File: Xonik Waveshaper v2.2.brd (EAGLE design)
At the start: 63.5 x 29.1 mm, 93 parts, among them IC1 TL074D, IC2 TL074D, IC3 TL074D, IC4 TL072D, IC5 4013D, IC6 LM311D, T1 2n3904

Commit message: Reduced footprints for op amps
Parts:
- added C15, C17, C18, C19: 1uF, rcl:C0402
- IC1, IC2, IC3: value TL074D -> TL074JT; device linear:SO14 -> joakim:TSSOP14J
- IC6: value LM311D -> LM311T; device linear:SO08 -> joakim:TSSOP8J
- moved IC6 78.2 mm to (51.4, 16.8), turned to 90 degrees
- moved C13 71.6 mm to (40.3, 21.7), turned to 90 degrees
- moved C12 59.1 mm to (23.5, 21.7), turned to 90 degrees
- moved C9 49.9 mm to (8.89, 21.7), turned to 90 degrees
- moved C16 12.6 mm to (40.4, 11.9), turned to 90 degrees
- moved C10 7.23 mm to (23.5, 11.9), turned to 90 degrees
- moved C11 7.19 mm to (8.89, 11.9), turned to 90 degrees
- moved 15 4.92 mm to (7.14, 24.8)
- moved +12V 2.54 mm to (49.5, 3.49)
- moved -12V 2.54 mm to (52.1, 3.49)
- moved GND 2.54 mm to (54.6, 3.49)
- moved IC4 1.84 mm to (46.7, 16.8)
- moved T1 1.59 mm to (4.13, 16.8)
- moved 13 1.11 mm to (10.6, 24.8)
- moved 5 1.11 mm to (10.6, 9.21)
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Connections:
- net N$20 renamed SS2_TRIM_R
- net N$23 renamed SS1_TRIM_L
- net N$28 renamed SS2_TRIM_L
- net N$33 renamed PW_CV
- net N$41 renamed SS1_TRIM_R
- net +12V: now also C15.2, C18.2
- net -12V: now also C17.1, C19.1
- net GND: now also C15.1, C17.2, C18.1, C19.2
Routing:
- net N$14: track 31.7 -> 36.9 mm
- net -12V: track 70.8 -> 75.7 mm
- net N$19: track 21.6 -> 24.8 mm
- net N$3: track 12.9 -> 9.76 mm
- net SUB_SAW_1: track 30.9 -> 33.6 mm
- net GND: track 256.1 -> 253.9 mm
- net N$13: track 19.0 -> 17.0 mm
- net SS2_TRIM_R: track 20.3 -> 22.2 mm
- net +12V: track 88.9 -> 90.7 mm
- net N$24: track 24.9 -> 23.1 mm
- net PULSE: track 23.3 -> 24.7 mm
- net TRIANGLE: track 33.0 -> 34.2 mm
- net N$12: track 11.2 -> 12.3 mm
- net N$4: track 21.2 -> 20.2 mm
- net SUB_SAW_2: track 24.1 -> 25.1 mm
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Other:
- board size 63.5 x 29.1 mm -> 63.5 x 29.3 mm

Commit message: Almost all tracing done!
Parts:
- 22: device resistor:R0805 -> rcl:R0603
- C1, C14, C2, C3, C4, C5, C6, C7: device rcl:C0603 -> joakim:R0603-J
- IC4: value TL072D -> TL072JT; device joakim:SO08J -> joakim:TSSOP8J
- IC5: value 4013D -> 4013T; device joakim:SO14J -> joakim:TSSOP14J
- moved 33 91.2 mm to (52.2, 10.5), turned to 90 degrees
- moved 1 91.1 mm to (48.7, 23.2), turned to 270 degrees
- moved C14 88.9 mm to (51.0, 23.2), turned to 90 degrees
- moved 2 86.1 mm to (50.0, 10.5), turned to 270 degrees
- moved 32 50.3 mm to (37.6, 10.5), turned to 270 degrees
- moved 21 33.2 mm to (17.5, 10.5), turned to 90 degrees
- moved 31 26.4 mm to (12.5, 10.5), turned to 270 degrees
- moved 9 21.1 mm to (12.5, 14.0), turned to 270 degrees
- moved 7 17.4 mm to (2.22, 19.1), turned to 0 degrees
- moved C8 17.1 mm to (48.4, 19.2), turned to 270 degrees
- moved 26 15.6 mm to (44.3, 23.2), turned to 270 degrees
- moved 8 15.1 mm to (2.22, 16.8), turned to 180 degrees
- moved 29 14.5 mm to (42.1, 23.2)
- moved C2 14.2 mm to (39.8, 23.2)
- moved C7 13.8 mm to (2.22, 14.6), turned to 180 degrees
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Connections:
- net GND: now also IC1.5; no longer IC1.3
- net INV_SAW: now also IC1.7; no longer IC1.1
- net N$1: now also IC2.2; no longer IC2.6
- net N$10: now also IC1.6; no longer IC1.2
- net N$15: now also IC2.6; no longer IC2.2
- net N$42: now also IC2.1; no longer IC2.7
- net N$5: now also IC1.3; no longer IC1.5
- net N$6: now also IC1.2; no longer IC1.6
- net PULSE: now also IC1.1; no longer IC1.7
- net SAW: now also IC2.7; no longer IC2.1
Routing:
- net GND: track 253.9 -> 42.4 mm, vias 22 -> 34
- net SUB_SAW_1: track 33.6 -> 5.00 mm, vias 2 -> 0
- net N$14: track 36.9 -> 9.64 mm
- net INV_SAW: track 50.2 -> 23.3 mm
- net N$35: track 46.5 -> 20.1 mm, vias 2 -> 0
- net SUB_SQR_1: track 47.1 -> 23.8 mm
- net SS2_TRIM_R: track 22.2 -> 0.00 mm, vias 2 -> 0
- net SS1_TRIM_R: track 23.7 -> 2.76 mm, vias 1 -> 0
- net SINE: track 35.7 -> 14.9 mm, vias 3 -> 2
- net SUB_SAW_2: track 25.1 -> 4.96 mm, vias 2 -> 0
- net SUB_SQR_2: track 30.1 -> 10.5 mm, vias 1 -> 0
- net +12V: track 90.7 -> 73.0 mm, vias 5 -> 0
- net N$36: track 21.0 -> 3.36 mm, vias 2 -> 1
- net PULSE: track 24.7 -> 7.43 mm, vias 1 -> 0
- net N$26: track 29.6 -> 15.6 mm
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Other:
- board size 63.5 x 29.3 mm -> 55.9 x 29.3 mm

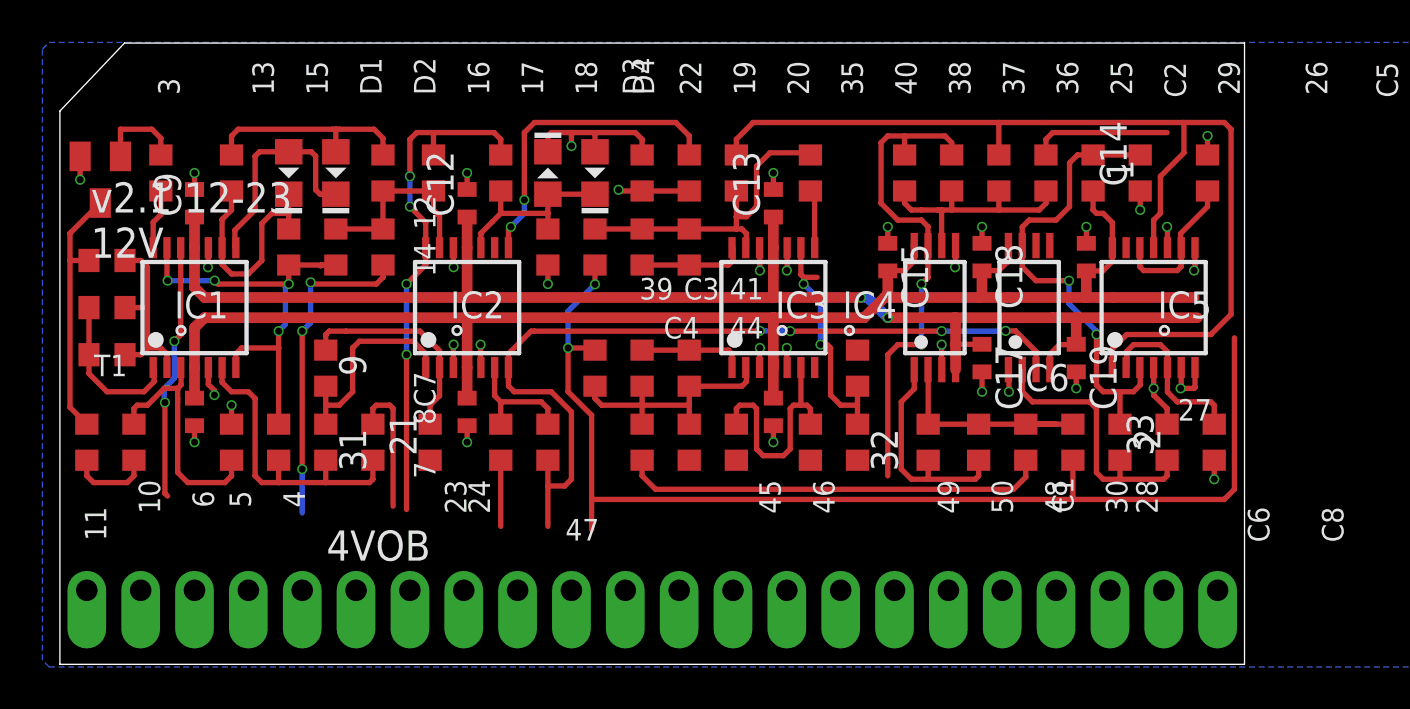
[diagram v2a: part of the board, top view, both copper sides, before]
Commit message: Finished tracing but not satisfied with placement of GND
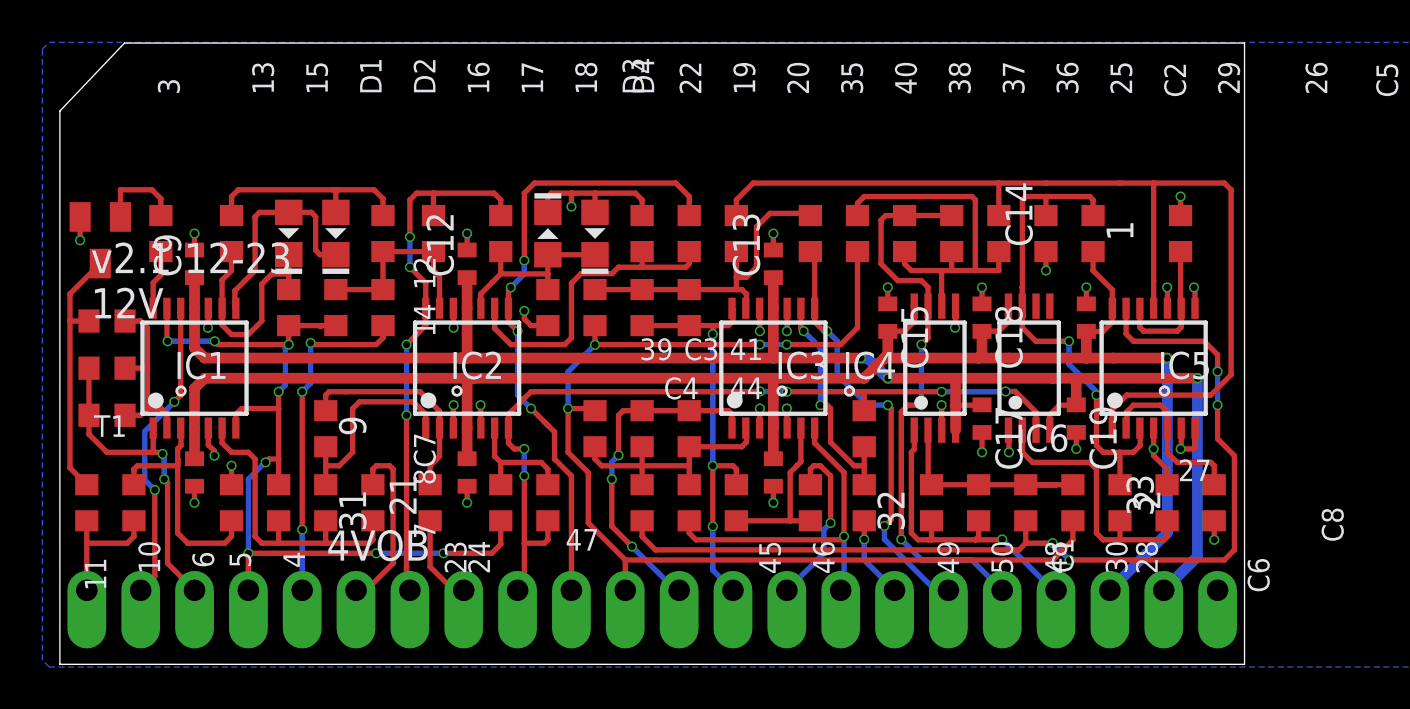
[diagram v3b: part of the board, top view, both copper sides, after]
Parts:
- moved IN_CENTER 17.8 mm to (19.1, 3.49)
- moved SUB_SQR_2 12.7 mm to (47.0, 3.49)
- moved ST3 10.2 mm to (34.3, 3.49)
- moved ST4 10.2 mm to (36.8, 3.49)
- moved DCO_IN 10.2 mm to (14.0, 3.49)
- moved 25 9.34 mm to (37.6, 20.3), turned to 90 degrees
- moved SUB_SQR_1 7.62 mm to (44.5, 3.49)
- moved INV_SAW 7.62 mm to (8.89, 3.49)
- moved PULSE 7.62 mm to (6.35, 3.49)
- moved C14 5.28 mm to (46.5, 20.3)
- moved PULSE_AMP_CV 5.08 mm to (1.27, 3.49)
- moved PW_CV 5.08 mm to (3.81, 3.49)
- moved TRIANGLE 5.08 mm to (16.5, 3.49)
- moved C5 3.13 mm to (52.9, 20.3)
- moved 35 2.88 mm to (37.9, 11.1)
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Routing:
- net N$35: track 20.1 -> 46.1 mm, vias 0 -> 4
- net SS1_TRIM_R: track 2.76 -> 20.0 mm, vias 0 -> 3
- net INV_SAW: track 23.3 -> 40.4 mm, vias 4 -> 8
- net SS2_TRIM_R: track 0.00 -> 16.5 mm, vias 0 -> 1
- net SUB_SAW_1: track 5.00 -> 19.8 mm, vias 0 -> 3
- net SINE: track 14.9 -> 29.6 mm, vias 2 -> 4
- net N$36: track 3.36 -> 14.8 mm, vias 1 -> 0
- net SUB_SAW_2: track 4.96 -> 16.0 mm, vias 0 -> 3
- net -12V: track 66.1 -> 76.9 mm, vias 2 -> 3
- net +12V: track 73.0 -> 83.6 mm, vias 0 -> 1
- net SS2_TRIM_L: track 0.00 -> 8.21 mm, vias 0 -> 1
- net PULSE: track 7.43 -> 15.3 mm, vias 0 -> 2
- net N$19: track 11.6 -> 18.3 mm
- net -2.5V: track 61.1 -> 54.4 mm, vias 2 -> 4
- net SUB_SQR_2: track 10.5 -> 14.7 mm, vias 0 -> 1
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
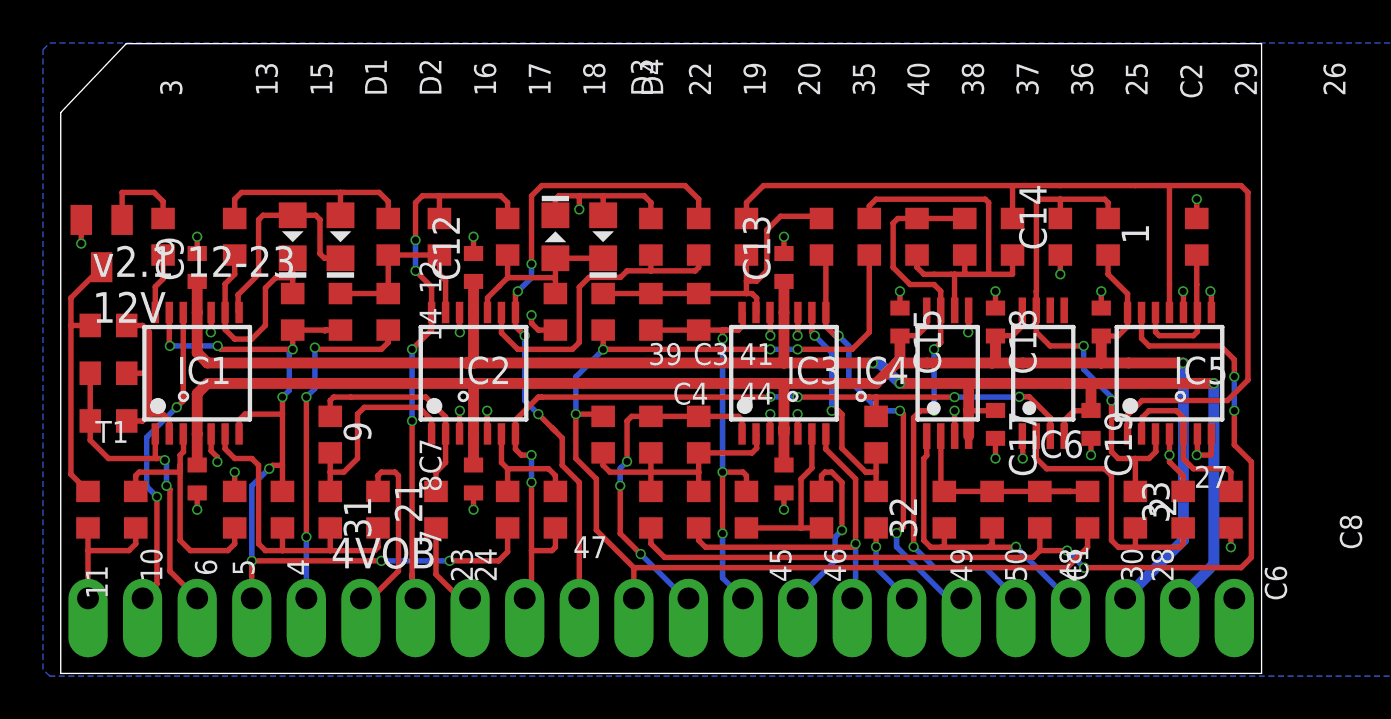
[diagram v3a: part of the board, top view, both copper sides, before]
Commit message: Fixed GND placement
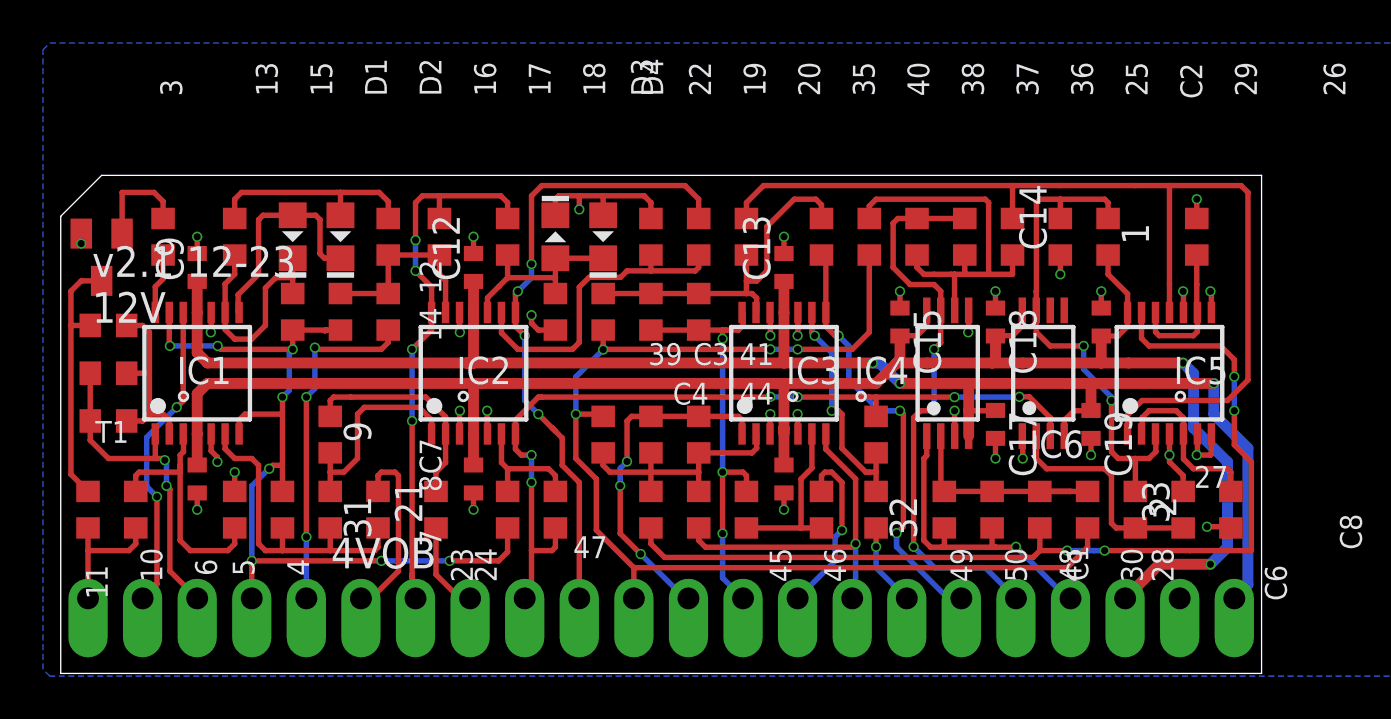
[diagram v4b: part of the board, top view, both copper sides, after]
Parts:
- moved -12V 2.54 mm to (54.6, 3.49)
- moved GND 2.54 mm to (52.1, 3.49)
- moved T1 0.64 mm to (1.91, 19.4)
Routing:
- net +12V: track 83.6 -> 86.7 mm, vias 1 -> 2
- net N$25: track 13.0 -> 10.6 mm
- net N$26: track 15.6 -> 16.7 mm
- net N$35: track 46.1 -> 45.3 mm
- net N$3: track 4.16 -> 4.79 mm
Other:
- board size 55.9 x 29.3 mm -> 55.9 x 23.2 mm

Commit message: Better ordering of outputs
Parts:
- moved INV_SAW 10.2 mm to (19.1, 3.49)
- moved IN_CENTER 5.08 mm to (14.0, 3.49)
- moved 31 2.54 mm to (15.1, 7.62)
- moved DCO_IN 2.54 mm to (11.4, 3.49)
- moved SYMMETRY 2.54 mm to (8.89, 3.49)
- moved 10 1.90 mm to (12.9, 7.62)
- moved 9 1.75 mm to (14.3, 11.1)
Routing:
- net N$1: track 10.2 -> 8.46 mm
- net N$42: track 9.86 -> 8.27 mm
- net IN_CENTER: track 4.21 -> 5.78 mm, vias 0 -> 1
- net SYMMETRY: track 16.0 -> 17.0 mm
- net INV_SAW: track 40.4 -> 39.4 mm, vias 8 -> 6
- net DCO_IN: track 8.54 -> 7.73 mm, vias 0 -> 1

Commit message: Trying to normalize
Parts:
- moved U$1 3.59 mm to (54.3, 13.5)
- moved 3 0.16 mm to (4.60, 20.3)
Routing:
- net N$22: track 10.9 -> 12.0 mm
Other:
- board text added: "+12V"
- board text added: "-12V"
- board text added: "-2.5V"
- board text added: "In center"
- board text added: "Saw 1"
- board text added: "Saw 2"
- board text added: "Waveshaper v2.2 March 24"
- board text removed: "+15V"
- board text removed: "+3V3"
- board text removed: "-15V"
- board text removed: "-2.5v"
- board text removed: "1"
- board text removed: "2"
- board text removed: "Center"
- board text removed: "Timer in"
- board text removed: "Waveshaper"
- board text removed: "v2.1 12-23 12V"
